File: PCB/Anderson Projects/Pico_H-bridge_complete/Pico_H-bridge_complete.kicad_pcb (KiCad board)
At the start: 4 copper layers, 83 x 65.5 mm, 75 parts, among them J1 Screw_Terminal_01x9, J2 Motor Connector, J3 Screw_Terminal_01x02, J4 2.54 header, Q1 AO3400A, Q2 AO3400A, Q3 DMP3130LQ-7, Q4 DMP3130LQ-7, Q5 MMBT3904, Q6 MMBT3904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

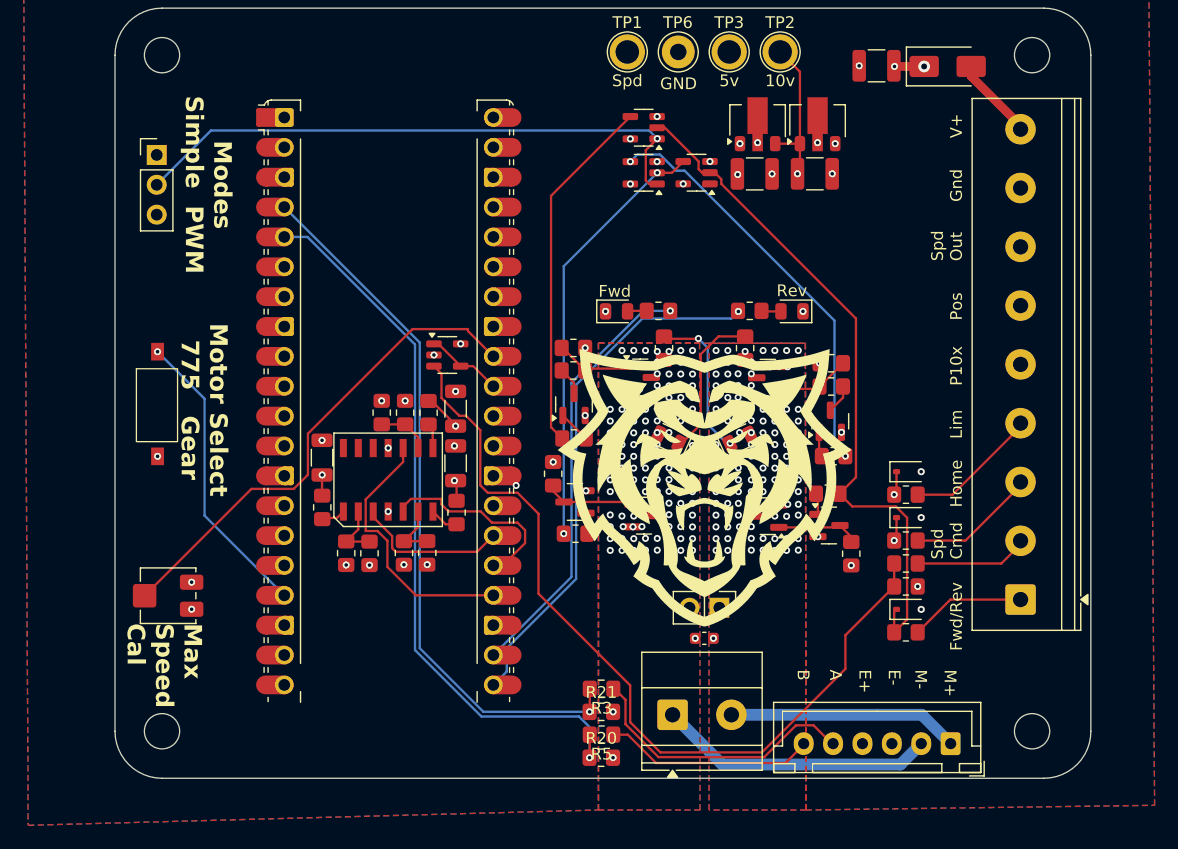
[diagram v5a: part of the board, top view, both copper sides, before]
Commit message: Anderson Motor Interface Board v2 complete and ordered.
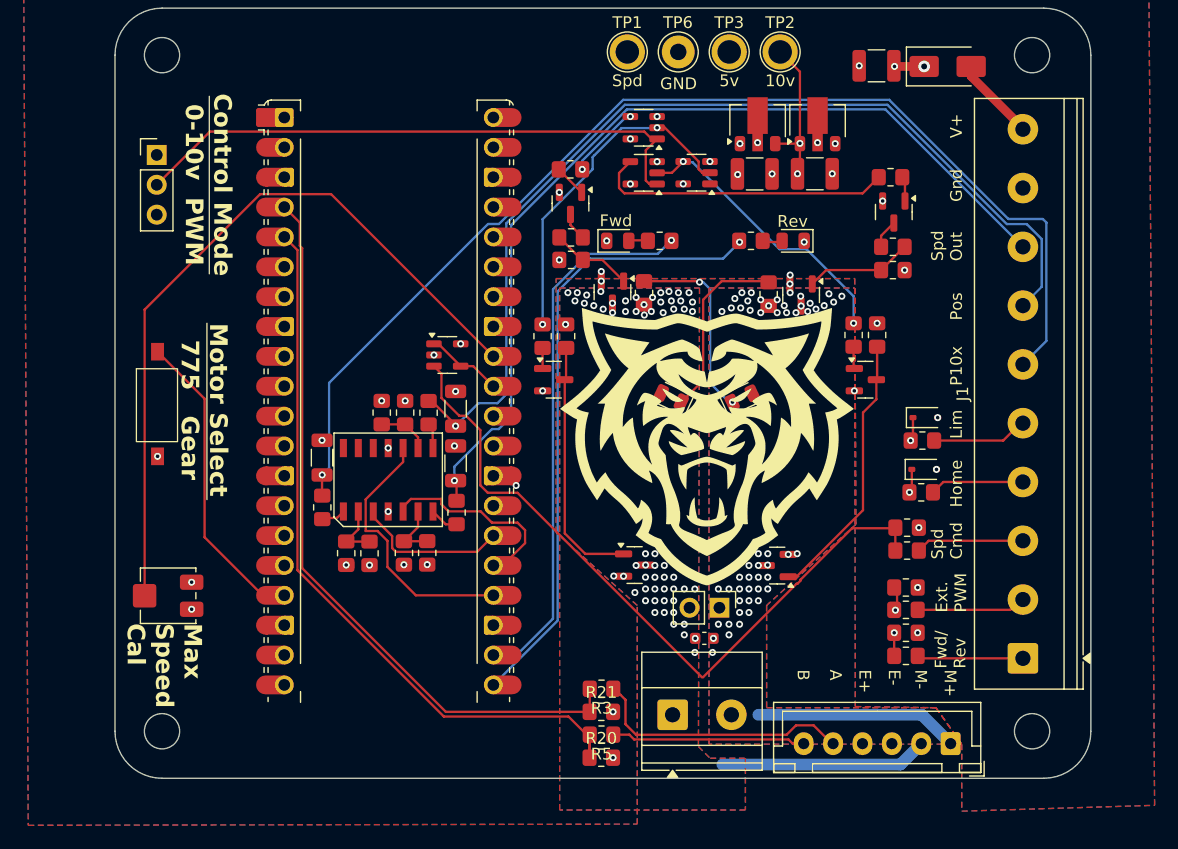
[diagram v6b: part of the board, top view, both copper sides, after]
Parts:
- removed D14: 5.1V, Diode_SMD:D_SOD-323
- added R32: 82k, Resistor_SMD:R_0805_2012Metric_Pad1.20x1.40mm_HandSolder, F.Cu at (150.3, 106.2)
- added R33: 22k, Resistor_SMD:R_0805_2012Metric_Pad1.20x1.40mm_HandSolder, F.Cu at (150.3, 104.3)
- added R34: 22k, Resistor_SMD:R_0805_2012Metric_Pad1.20x1.40mm_HandSolder, F.Cu at (150.3, 108.1)
- D3, D4: value LED_G -> LED_Y
- J1: footprint TerminalBlock_Phoenix:TerminalBlock_Phoenix_PT-1,5-9-5.0-H_1x09_P5.00mm_Horizontal -> TerminalBlock_Phoenix:TerminalBlock_Phoenix_PT-1,5-10-5.0-H_1x10_P5.00mm_Horizontal
- Q3, Q4: value DMP3130LQ-7 -> DMP3099L-7
- R1, R2: value 330Ω -> 330
- R10: value 3.9k -> 82k
- R20, R21: value 3.3kΩ -> 3.3k
- R22, R29: value 150Ω -> 150
- R23, R30: value 1kΩ -> 1k
- R26, R27, R31, R8: value 22kΩ -> 22k
- R3, R5: value 1.8kΩ -> 1.8k
- moved R8 24.2 mm to (149.0, 69.4), turned to 180 degrees
- moved R31 22.9 mm to (121.7, 68.7), turned to 180 degrees
- moved R28 18.7 mm to (147.8, 82.8), turned to -90 degrees
- moved Q6 18.6 mm to (149.2, 72.3), turned to -90 degrees
- moved Q5 17.1 mm to (121.7, 71.6), turned to -90 degrees
- moved R26 17.0 mm to (119.4, 82.9), turned to -90 degrees
- moved R27 13.7 mm to (145.8, 82.8), turned to -90 degrees
- moved R22 13.0 mm to (149.2, 75.3), turned to 180 degrees
- moved Q8 12.8 mm to (146.8, 86.6)
- moved R35 11.8 mm to (121.4, 82.9)
- moved R29 11.3 mm to (121.8, 74.5), turned to 180 degrees
- moved Q7 10.6 mm to (120.3, 86.6), turned to 0 degrees
- moved R23 9.50 mm to (149.2, 77.3), turned to 0 degrees
- moved Q3 7.63 mm to (125.3, 79.2), turned to -90 degrees
- moved Q4 7.59 mm to (141.4, 79.4), turned to -90 degrees
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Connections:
- J1 pad 5: Analog Position x10 -> Net-(J1-Pin_5)
- J1 pad 6: Analog Position -> Analog Position x10
- J1 pad 7: Analog Speed -> Analog Position
- J1 pad 8: GND -> Analog Speed
- J1 pad 9: Net-(D5-A) -> GND
- JP1 pad 3: +5V -> External PWM
- R25 pad 2: Net-(J1-Pin_2) -> Net-(J1-Pin_3)
- R26 pad 1: /H-Bridge/CCW1 -> Fwd/Rev
- R27 pad 1: Fwd/Rev -> /H-Bridge/CW1
- R4 pad 1: Net-(J1-Pin_3) -> Net-(J1-Pin_4)
- R6 pad 1: Net-(J1-Pin_4) -> Net-(J1-Pin_5)
- U10 pad 4: /H-Bridge/CCW1 -> /H-Bridge/CW1
- U8 pad 2: /H-Bridge/CCW1 -> /H-Bridge/CW1
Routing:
- net External PWM: track 0.00 -> 93.0 mm, vias 0 -> 1
- net /H-Bridge/CCW1: track 36.6 -> 0.00 mm, vias 2 -> 0
- net /H-Bridge/CW0: track 30.6 -> 6.38 mm, vias 0 -> 2
- net /H-Bridge/CW1: track 0.00 -> 24.1 mm, vias 0 -> 2
- net Net-(U1-GPIO27_ADC1): track 42.2 -> 63.8 mm
- net Limit Switch: track 61.8 -> 81.6 mm
- net +10V: track 107.6 -> 91.6 mm, vias 4 -> 5
- net Net-(Q2-G): track 7.06 -> 23.1 mm
- net Analog Position x10: track 83.2 -> 97.9 mm
- net Net-(Q1-G): track 7.74 -> 21.5 mm
- net Fwd/Rev: track 58.6 -> 72.0 mm, vias 0 -> 3
- net Home: track 59.0 -> 70.8 mm
- net Net-(U11-+): track 72.0 -> 61.4 mm
- net /H-Bridge/CCW0: track 35.4 -> 25.5 mm, vias 2 -> 0
- net Net-(U1-GPIO17): track 36.8 -> 46.4 mm
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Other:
- board text added: "4"
- board text added: "83.00 mm x 65.50 mm"
- board text added: "Control Mode 0-10v PWM"
- board text added: "Ext. PWM"
- board text added: "Fwd/ Rev"
- board text added: "PLC Motor Interface Board Anderson - rev2 July 2025"
- board text removed: "120.2500 mm x 65.5000 mm"
- board text removed: "2"
- board text removed: "Fwd/Rev"
- board text removed: "Modes Simple PWM"
- board text removed: "PLC Motor Interface Board Anderson - rev1 July 2025"

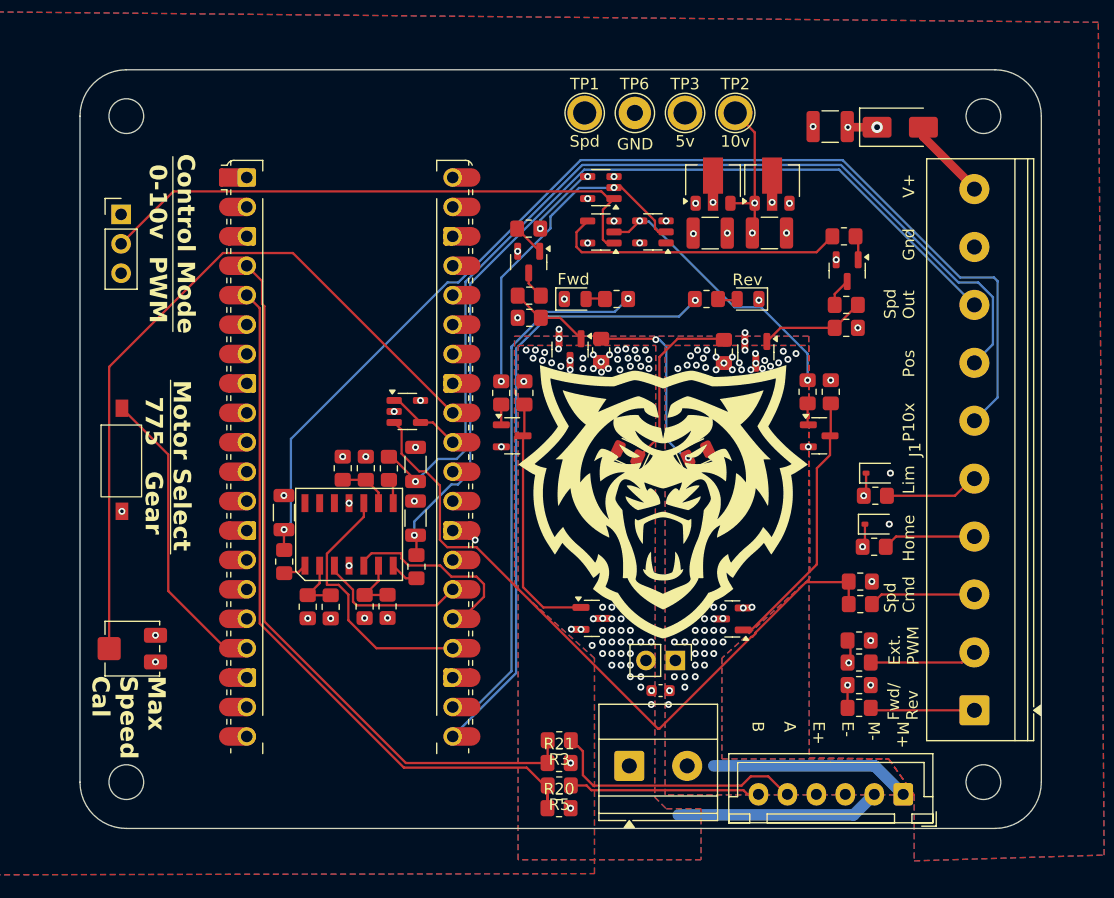
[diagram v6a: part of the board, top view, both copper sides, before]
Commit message: Anderson Motor Interface Board v3. - Bengal eyes LED for both directions - heatsink pads on back of board - DIN rail mount Added Heater Box Schematic files in Documentation
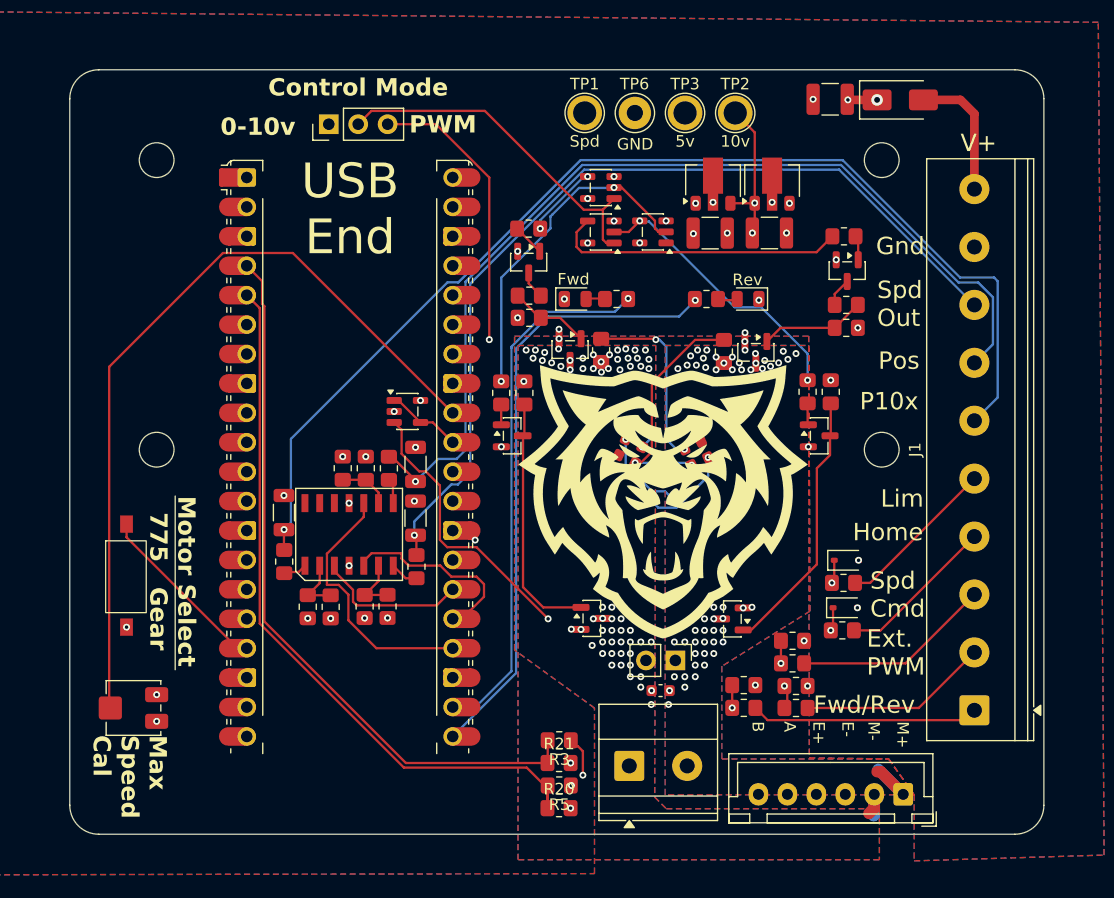
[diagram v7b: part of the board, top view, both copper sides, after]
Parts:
- added D8: LED_W, LED_SMD:LED_0603_1608Metric, F.Cu at (136.5, 88.8)
- added D9: LED_W, LED_SMD:LED_0603_1608Metric, F.Cu at (130.2, 88.6)
- D3, D4: footprint LED_SMD:LED_0805_2012Metric -> LED_SMD:LED_0603_1608Metric
- moved JP1 19.5 mm to (104.5, 59.7), turned to 90 degrees
- moved SW1 10.0 mm to (87.0, 98.7)
- moved R10 9.96 mm to (140.3, 110.1)
- moved R34 9.96 mm to (140.3, 108.1)
- moved D7 8.01 mm to (149.2, 97.3)
- moved R6 8.01 mm to (148.9, 99.3)
- moved R24 7.77 mm to (144.5, 104.3)
- moved R25 7.77 mm to (144.5, 106.2)
- moved R4 7.72 mm to (148.8, 103.4)
- moved D6 7.72 mm to (149.1, 101.4)
- moved R32 6.72 mm to (144.8, 110.1)
- moved R33 6.72 mm to (144.8, 108.2)
- moved RV1 5.13 mm to (87.6, 110.1)
- moved C4 2.36 mm to (147.8, 57.5)
- moved D5 2.36 mm to (153.8, 57.6)
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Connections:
- D3 pad 2: M- -> M+
- D4 pad 1: Net-(D4-K) -> Net-(D3-K)
- R7 pad 1: Net-(D4-K) -> Net-(D3-K)
- R9 pad 2: Net-(D3-K) -> Net-(D8-K)
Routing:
- net External PWM: track 93.0 -> 70.6 mm, vias 1 -> 2
- net Net-(D8-K): track 0.00 -> 20.5 mm, vias 0 -> 2
- net Net-(JP1-C): track 49.7 -> 30.2 mm
- net Net-(D4-K): track 16.5 -> 0.00 mm, vias 2 -> 0
- net Net-(U1-GPIO13): track 26.3 -> 14.7 mm
- net Speed_set PWM: track 53.3 -> 42.1 mm
- net Net-(J1-Pin_1): track 9.04 -> 19.7 mm
- net Limit Switch: track 81.6 -> 72.1 mm
- net Net-(U11-+): track 61.4 -> 52.6 mm, vias 0 -> 2
- net Home: track 70.8 -> 62.4 mm
- net Net-(J1-Pin_3): track 9.20 -> 17.2 mm
- net Fwd/Rev: track 72.0 -> 79.3 mm
- net Net-(J1-Pin_2): track 9.21 -> 16.4 mm
- net M-: track 17.7 -> 11.7 mm, vias 58 -> 60
- net Net-(J1-Pin_5): track 8.16 -> 14.0 mm
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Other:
- board size 83 x 65.5 mm -> 84.1 x 66 mm
- board text added: "0-10v"
- board text added: "Control Mode"
- board text added: "Fwd/Rev"
- board text added: "PLC Motor Interface Board Anderson - rev3 Nov 2025"
- board text added: "PWM"
- board text added: "USB End"
- board text removed: "Control Mode 0-10v PWM"
- board text removed: "Fwd/ Rev"
- board text removed: "PLC Motor Interface Board Anderson - rev2 July 2025"
